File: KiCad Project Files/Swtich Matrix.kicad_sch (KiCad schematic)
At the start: 147 parts

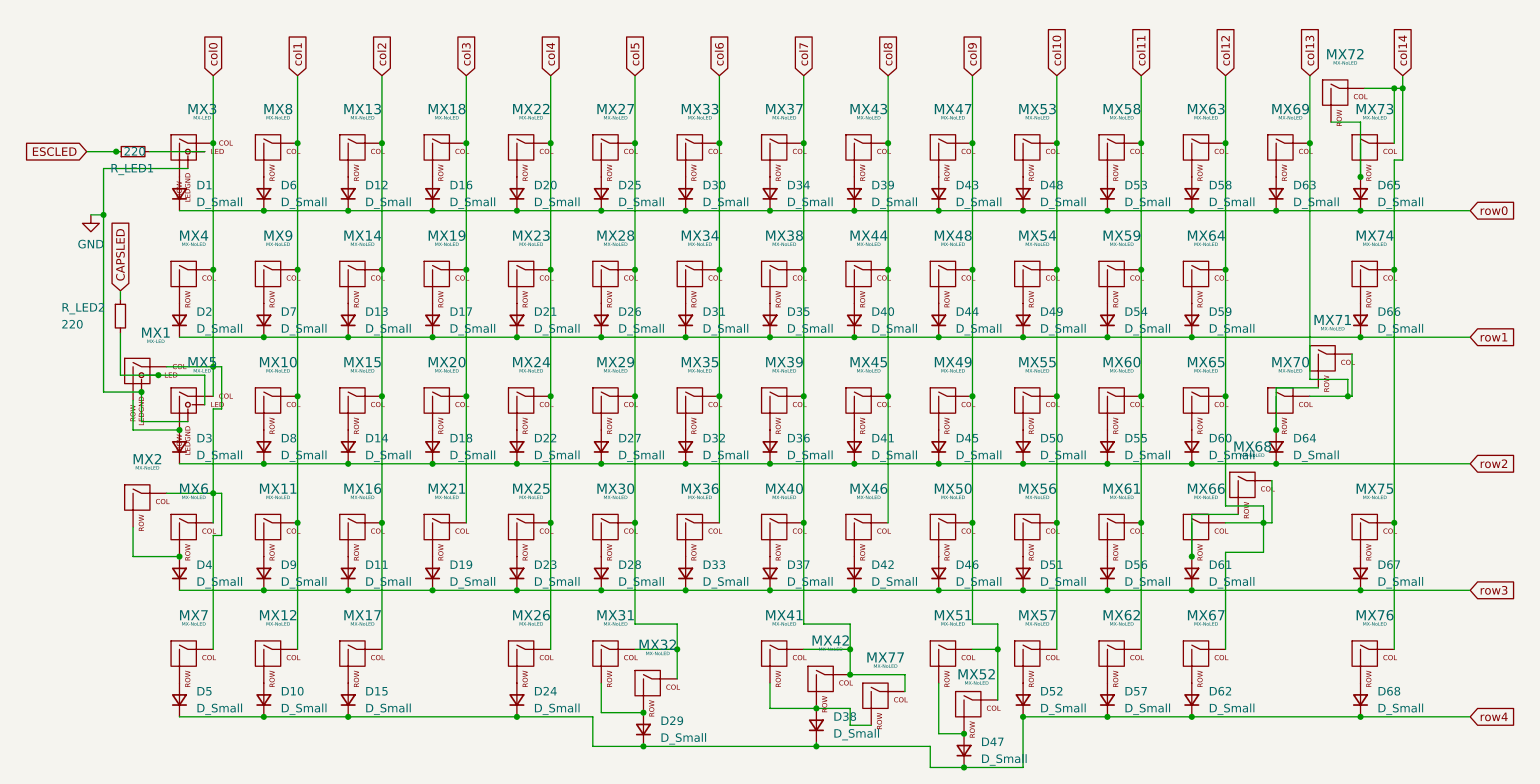
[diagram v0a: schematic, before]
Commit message: Initial Modifications
Summary of changes from original SST60:
-Removes extraneous keys, opting for ANSI-only, split right shift, split Backspace, 7U space bar, stepped caps lock.
-Switched from MX-ANSI hybrid to MX-only
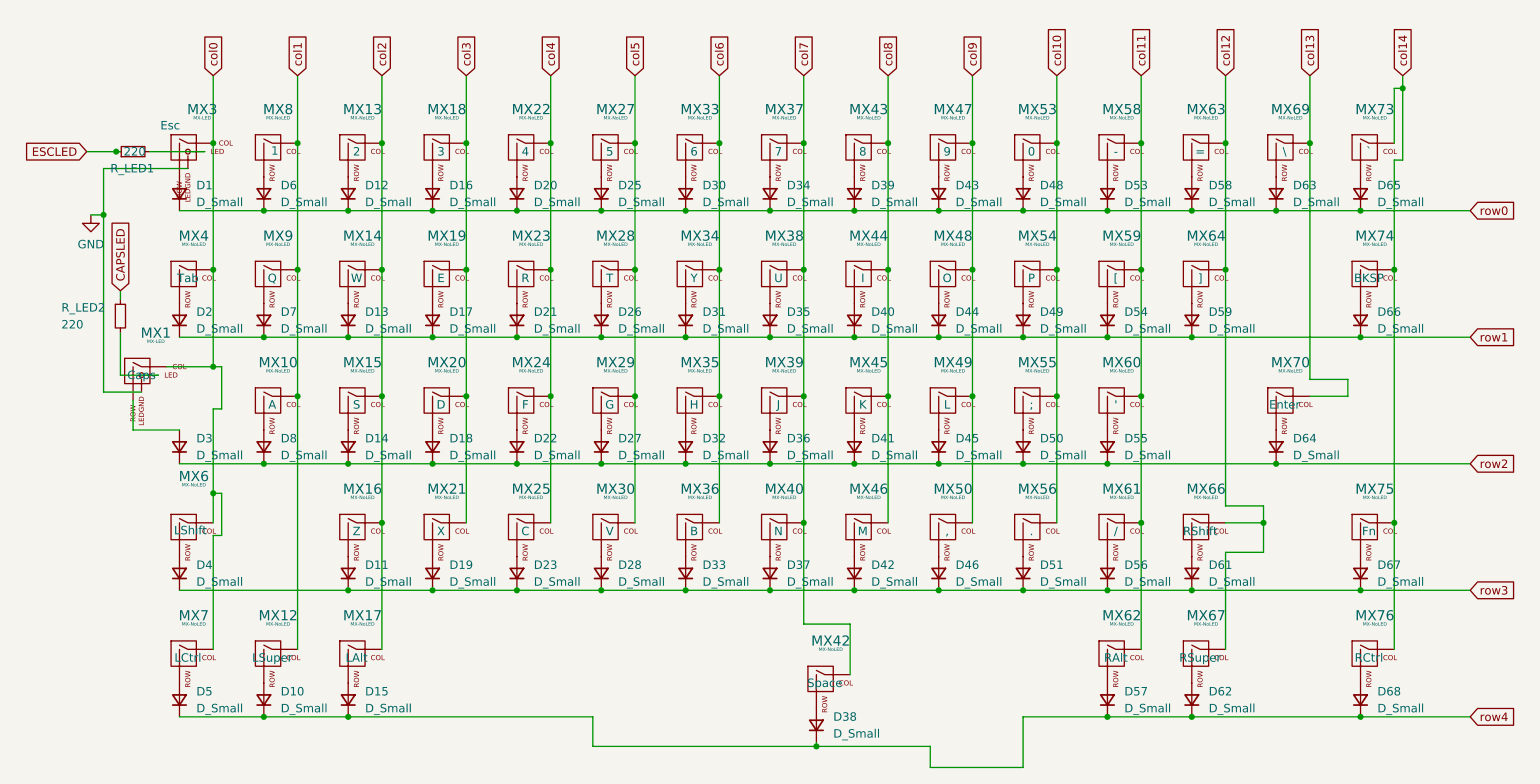
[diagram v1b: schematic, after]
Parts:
- removed D24, D29, D47, D52, D60, D9: D_Small, Diode_SMD:D_SOD-123, symbol Device:D_Small
- removed MX11, MX26, MX41, MX57, MX65: MX-NoLED, MX_Alps_Hybrid:MX-1U-NoLED, symbol cipulot_parts:MX-NoLED
- removed MX2: MX-NoLED, MX_Alps_Hybrid:MX-1.25U-NoLED, symbol cipulot_parts:MX-NoLED
- removed MX31: MX-NoLED, MX_Alps_Hybrid:MX-2.25U-ReversedStabilizers-NoLED, symbol cipulot_parts:MX-NoLED
- removed MX32, MX52: MX-NoLED, MX_Alps_Hybrid:MX-3U-ReversedStabilizers-NoLED, symbol cipulot_parts:MX-NoLED
- removed MX5: MX-LED, MX_Alps_Hybrid:MX-1.75U, symbol cipulot_parts:MX-LED
- removed MX51: MX-NoLED, MX_Alps_Hybrid:MX-2.75U-ReversedStabilizers-NoLED, symbol cipulot_parts:MX-NoLED
- removed MX68: MX-NoLED, MX_Alps_Hybrid:MX-2.75U-NoLED, symbol cipulot_parts:MX-NoLED
- removed MX71: MX-NoLED, MX_Alps_Hybrid:MX-ISO-ReversedStabilizers, symbol cipulot_parts:MX-NoLED
- removed MX72: MX-NoLED, MX_Alps_Hybrid:MX-2U-NoLED, symbol cipulot_parts:MX-NoLED
- removed MX77: MX-NoLED, MX_Alps_Hybrid:MX-10U-ReversedStabilizers-NoLED, symbol cipulot_parts:MX-NoLED
- MX1: footprint MX_Alps_Hybrid:MX-1.25U-FLIPPED -> MX_Only:MXOnly-1.25U
- MX10, MX12, MX13, MX14, MX15, MX16, MX18, MX19, MX20, MX21, MX22, MX23, MX24, MX25, MX27, MX28, MX29, MX30, MX33, MX34, MX35, MX36, MX37, MX38, MX39, MX40, MX43, MX44, MX45, MX46, MX47, MX48, MX49, MX50, MX53, MX54, MX55, MX56, MX58, MX59, MX60, MX61, MX63, MX64, MX67, MX69, MX73, MX75, MX8, MX9: footprint MX_Alps_Hybrid:MX-1U-NoLED -> MX_Only:MXOnly-1U-NoLED
- MX17, MX4, MX62, MX7, MX74, MX76: footprint MX_Alps_Hybrid:MX-1.5U-NoLED -> MX_Only:MXOnly-1.5U-NoLED
- MX3: footprint MX_Alps_Hybrid:MX-1U -> MX_Only:MXOnly-1U
- MX42: footprint MX_Alps_Hybrid:MX-7U-ReversedStabilizers-NoLED -> MX_Only:MXOnly-7U-ReversedStabilizers-NoLED
- MX6, MX70: footprint MX_Alps_Hybrid:MX-2.25U-NoLED -> MX_Only:MXOnly-2.25U-NoLED
- MX66: footprint MX_Alps_Hybrid:MX-1.75U-NoLED -> MX_Only:MXOnly-1.75U-NoLED

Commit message: Component updates
Updates to components to facilitate JLC PCB process.
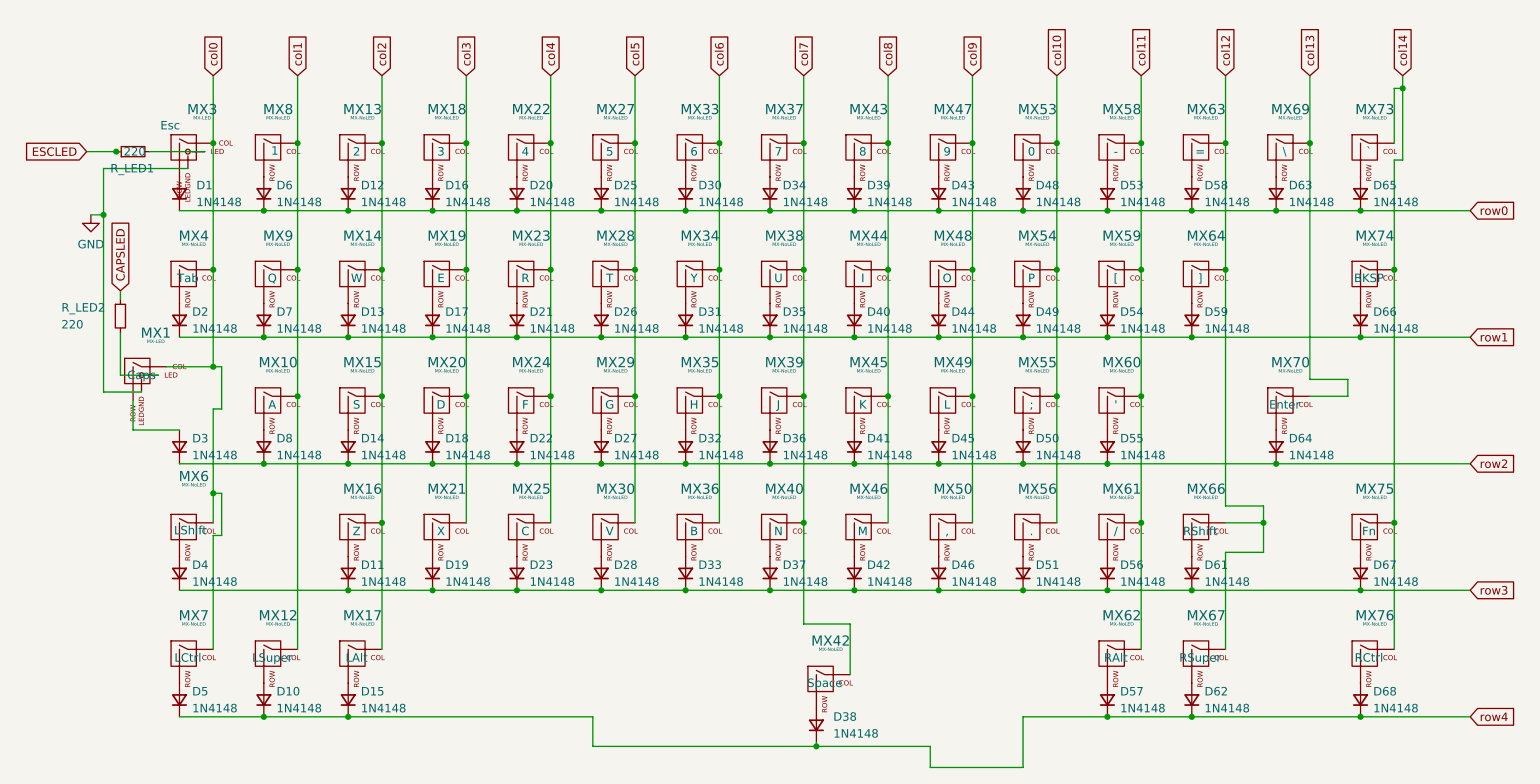
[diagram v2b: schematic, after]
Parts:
- D1, D10, D11, D12, D13, D14, D15, D16, D17, D18, D19, D2, D20, D21, D22, D23, D25, D26, D27, D28, D3, D30, D31, D32, D33, D34, D35, D36, D37, D38, D39, D4, D40, D41, D42, D43, D44, D45, D46, D48, D49, D5, D50, D51, D53, D54, D55, D56, D57, D58, D59, D6, D61, D62, D63, D64, D65, D66, D67, D68, D7, D8: value D_Small -> 1N4148
- MX1, MX10, MX12, MX13, MX14, MX15, MX16, MX17, MX18, MX19, MX20, MX21, MX22, MX23, MX24, MX25, MX27, MX28, MX29, MX3, MX30, MX33, MX34, MX35, MX36, MX37, MX38, MX39, MX4, MX40, MX42, MX43, MX44, MX45, MX46, MX47, MX48, MX49, MX50, MX53, MX54, MX55, MX56, MX58, MX59, MX6, MX60, MX61, MX62, MX63, MX64, MX66, MX67, MX69, MX7, MX70, MX73, MX74, MX75, MX76, MX8, MX9: now left out of the parts list
